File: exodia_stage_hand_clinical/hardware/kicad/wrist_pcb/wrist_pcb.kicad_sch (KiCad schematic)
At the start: 11 parts, among them J1 USBC_CONN, J2 ZIF_5PIN, Q1 IRLZ44N, Q2 2N7002, Q3 2N7002, Q4 2N7002, Q5 2N7002, U1 ESP32S3_MODULE, U2 TP4056_IC

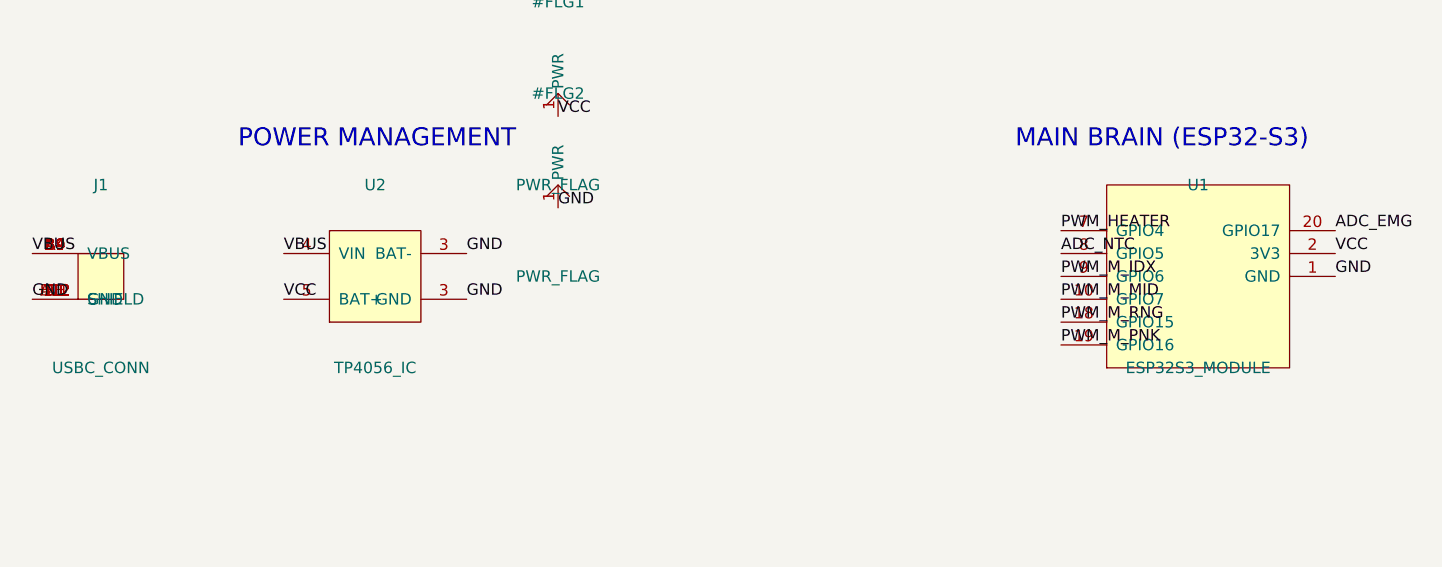
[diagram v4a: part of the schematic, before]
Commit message: Update physical ESP32 pin mappings (28/29/30/64/45) and exact USB pad mapping
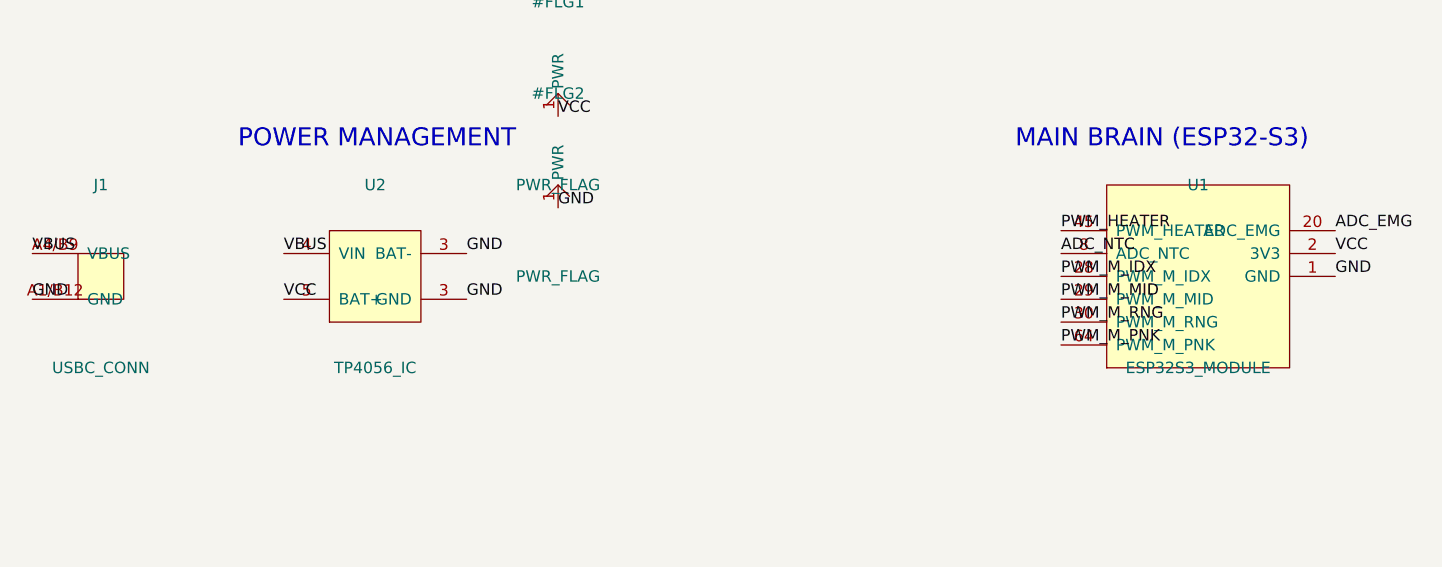
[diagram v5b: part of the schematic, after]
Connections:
- net GND: now also J1.A1/B12 (GND), J1.A12/B1 (GND); no longer J1.A1 (GND), J1.A12 (GND), J1.B1 (GND), J1.B12 (GND)
- net PWM_HEATER: now also U1.45 (PWM_HEATER); no longer U1.7 (GPIO4)
- net PWM_M_IDX: now also U1.28 (PWM_M_IDX); no longer U1.9 (GPIO6)
- net PWM_M_MID: now also U1.29 (PWM_M_MID); no longer U1.10 (GPIO7)
- net PWM_M_PNK: now also U1.64 (PWM_M_PNK); no longer U1.19 (GPIO16)
- net PWM_M_RNG: now also U1.30 (PWM_M_RNG); no longer U1.18 (GPIO15)
- net VBUS: now also J1.A4/B9 (VBUS), J1.A9/B4 (VBUS); no longer J1.A4 (VBUS), J1.A9 (VBUS), J1.B4 (VBUS), J1.B9 (VBUS)
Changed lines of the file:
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@@
     (title "Exodia Stage Hand - Clinical Wrist PCB")
     (date "2026-05-15")
-    (rev "v1.3")
+    (rev "v1.4")
     (company "Resonanx")
   )

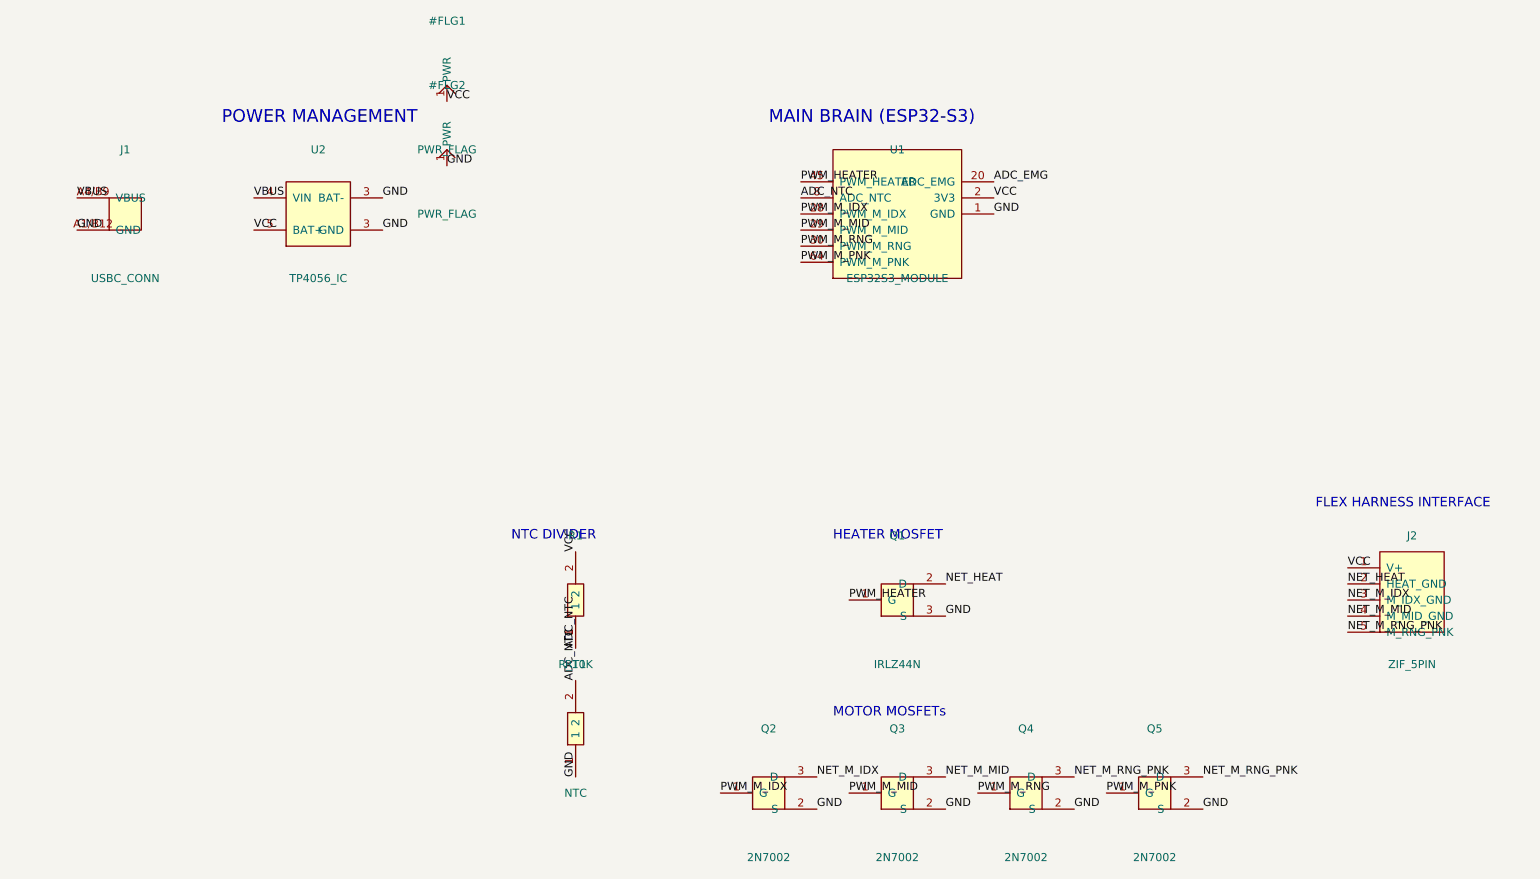
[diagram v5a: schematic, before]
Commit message: Schematic v1.6: 16-pin USB, LDO, Gate Resistors, CC Resistors
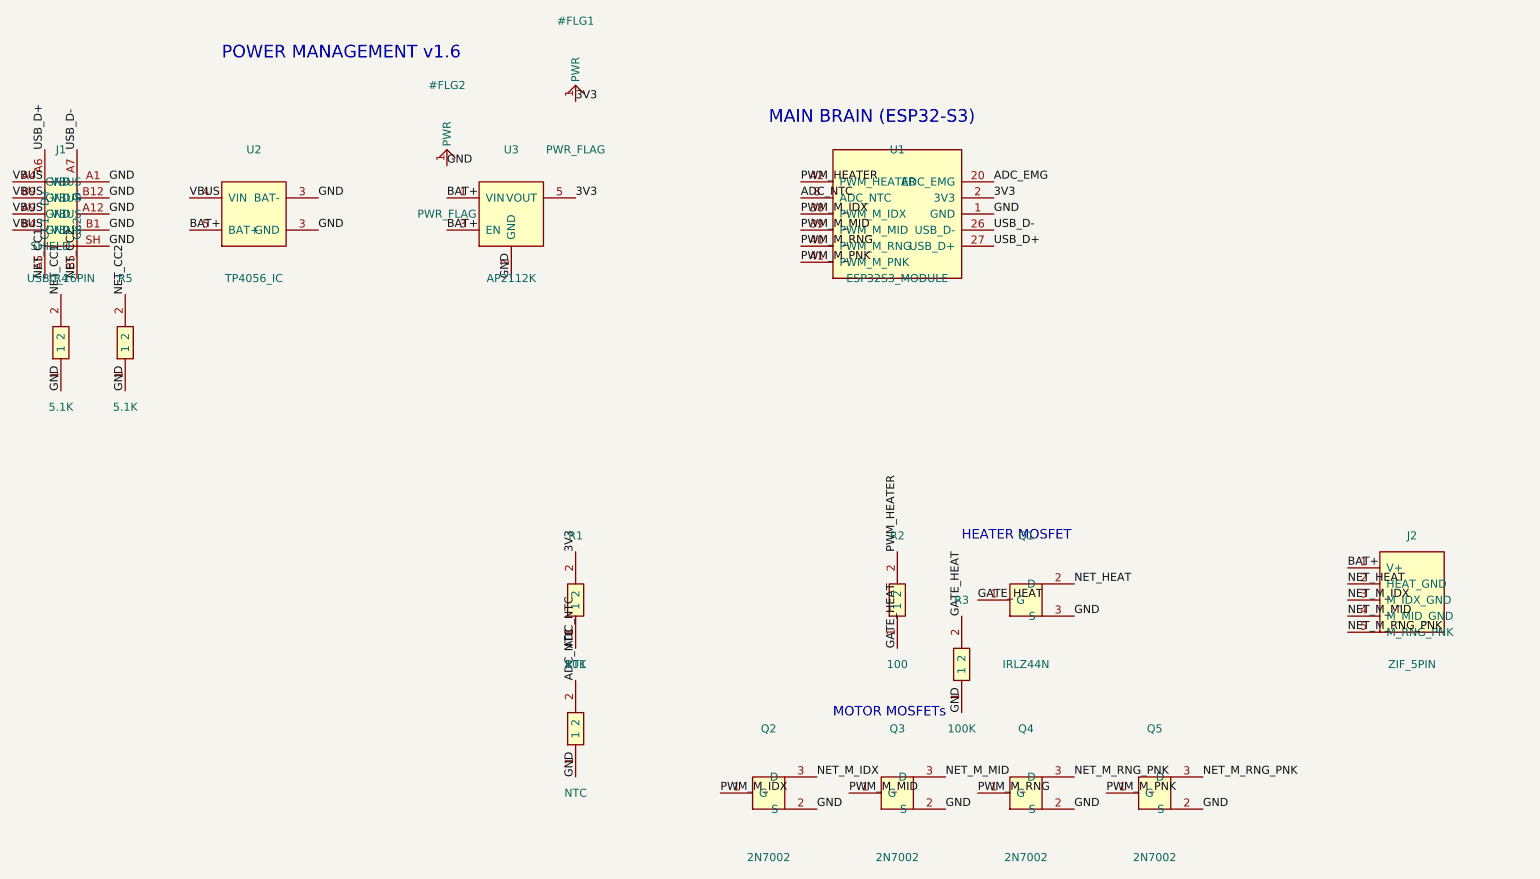
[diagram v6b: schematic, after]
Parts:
- removed J1: USBC_CONN, symbol USBC_CONN
- removed R1: R_10K, symbol R_10K
- added J1: USBC_16PIN, symbol USBC_16PIN
- added R1: 10K, symbol RESISTOR
- added R2: 100, symbol RESISTOR
- added R3: 100K, symbol RESISTOR
- added R4, R5: 5.1K, symbol RESISTOR
- added U3: AP2112K, symbol AP2112K
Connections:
- net ADC_NTC: now also R1.1
- net GND: now also J1.A1 (GND), J1.A12 (GND), J1.B1 (GND), J1.B12 (GND), J1.SH (SHIELD), R3.1, R4.1, R5.1, U3.2 (GND)
- net PWM_HEATER: now also U1.42 (PWM_HEATER), R2.2; no longer Q1.1 (G), U1.45 (PWM_HEATER)
- net PWM_M_IDX: now also U1.38 (PWM_M_IDX); no longer U1.28 (PWM_M_IDX)
- net PWM_M_MID: now also U1.39 (PWM_M_MID); no longer U1.29 (PWM_M_MID)
- net PWM_M_PNK: now also U1.41 (PWM_M_PNK); no longer U1.64 (PWM_M_PNK)
- net PWM_M_RNG: now also U1.40 (PWM_M_RNG); no longer U1.30 (PWM_M_RNG)
- net VBUS: now also J1.A4 (VBUS), J1.A9 (VBUS), J1.B4 (VBUS), J1.B9 (VBUS)
- net VCC renamed BAT+
- net BAT+: now also U3.1 (VIN), U3.3 (EN); no longer U1.2 (3V3)
- new net 3V3: R1.2, U1.2 (3V3), U3.5 (VOUT)
- new net GATE_HEAT: Q1.1 (G), R2.1, R3.2
- new net NET_CC1: J1.A5 (CC1), R4.2
- new net NET_CC2: J1.B5 (CC2), R5.2
- new net USB_D+: J1.A6 (D+), U1.27 (USB_D+)
- new net USB_D-: J1.A7 (D-), U1.26 (USB_D-)
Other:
- note added: "POWER MANAGEMENT v1.6"
- note removed: "FLEX HARNESS INTERFACE"
- note removed: "NTC DIVIDER"
- note removed: "POWER MANAGEMENT"

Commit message: PCB v1.6: Wiped traces, auto-placed new components
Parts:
- J1, U2: footprint (none) -> Connector_USB:USB_C_Receptacle_XKB_U262-16XN-4BVC11
- J2: footprint (none) -> Connector_FFC-FPC:TE_84952-5_1x05-1MP_P1.0mm_Horizontal
- Q1: footprint (none) -> Package_TO_SOT_SMD:TO-252-2
- Q2, Q3, Q4, Q5: footprint (none) -> Package_TO_SOT_SMD:SOT-23
- R1, R2, R3, R4, R5, RT1: footprint (none) -> Resistor_SMD:R_0603_1608Metric
- U1: footprint (none) -> RF_Module:ESP32-S2-MINI-1
- U3: footprint (none) -> Package_TO_SOT_SMD:SOT-23-5

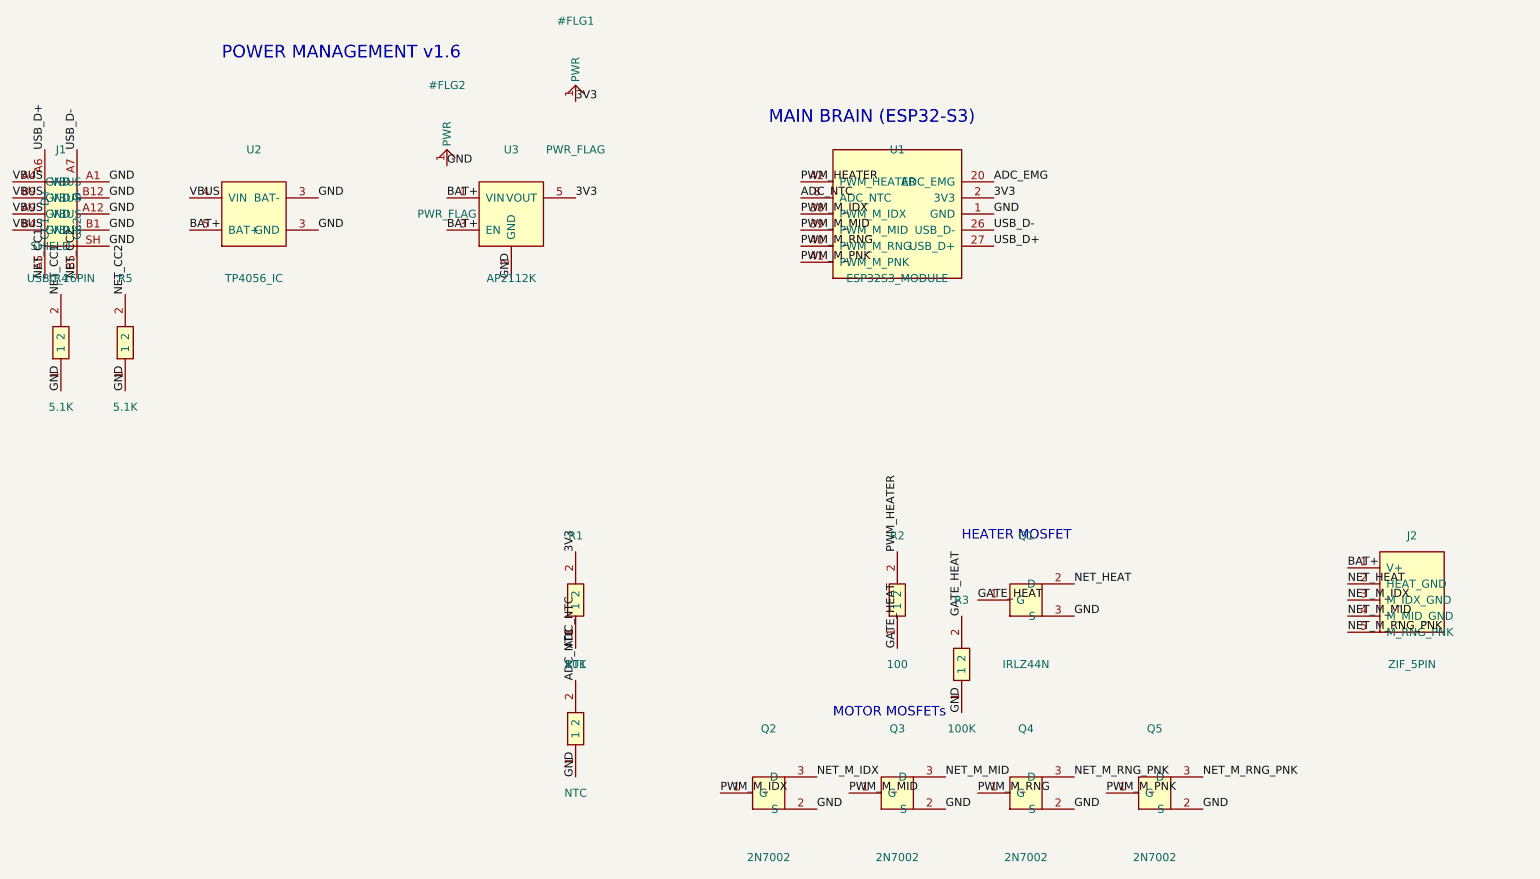
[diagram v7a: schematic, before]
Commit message: Schematic v1.7: AO3400A Heater MOSFET, Netclasses (power_high, signal_data)
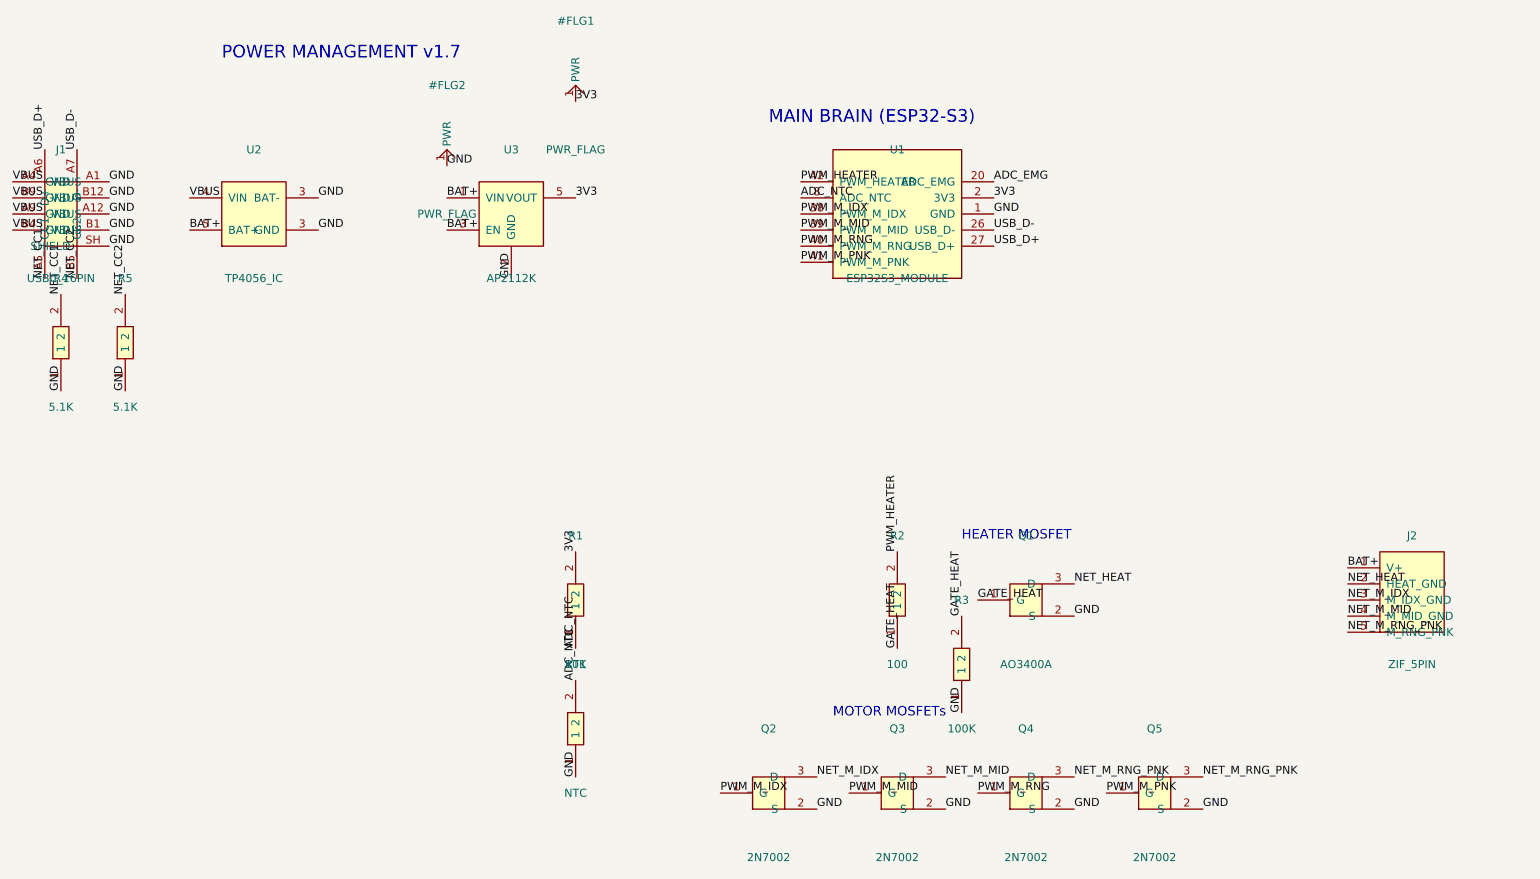
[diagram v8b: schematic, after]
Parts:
- removed Q1: IRLZ44N, Package_TO_SOT_SMD:TO-252-2, symbol IRLZ44N
- added Q1: AO3400A, symbol AO3400A
- J1, U2: footprint Connector_USB:USB_C_Receptacle_XKB_U262-16XN-4BVC11 -> (none)
- J2: footprint Connector_FFC-FPC:TE_84952-5_1x05-1MP_P1.0mm_Horizontal -> (none)
- Q2, Q3, Q4, Q5: footprint Package_TO_SOT_SMD:SOT-23 -> (none)
- R1, R2, R3, R4, R5, RT1: footprint Resistor_SMD:R_0603_1608Metric -> (none)
- U1: footprint RF_Module:ESP32-S2-MINI-1 -> (none)
- U3: footprint Package_TO_SOT_SMD:SOT-23-5 -> (none)
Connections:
- net GATE_HEAT: now also Q1.1 (G)
- net GND: now also Q1.2 (S)
- net NET_HEAT: now also Q1.3 (D)
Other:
- note added: "POWER MANAGEMENT v1.7"
- note removed: "POWER MANAGEMENT v1.6"
